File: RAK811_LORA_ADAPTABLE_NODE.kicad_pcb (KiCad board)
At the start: 2 copper layers, 75 x 49 mm, 6 parts

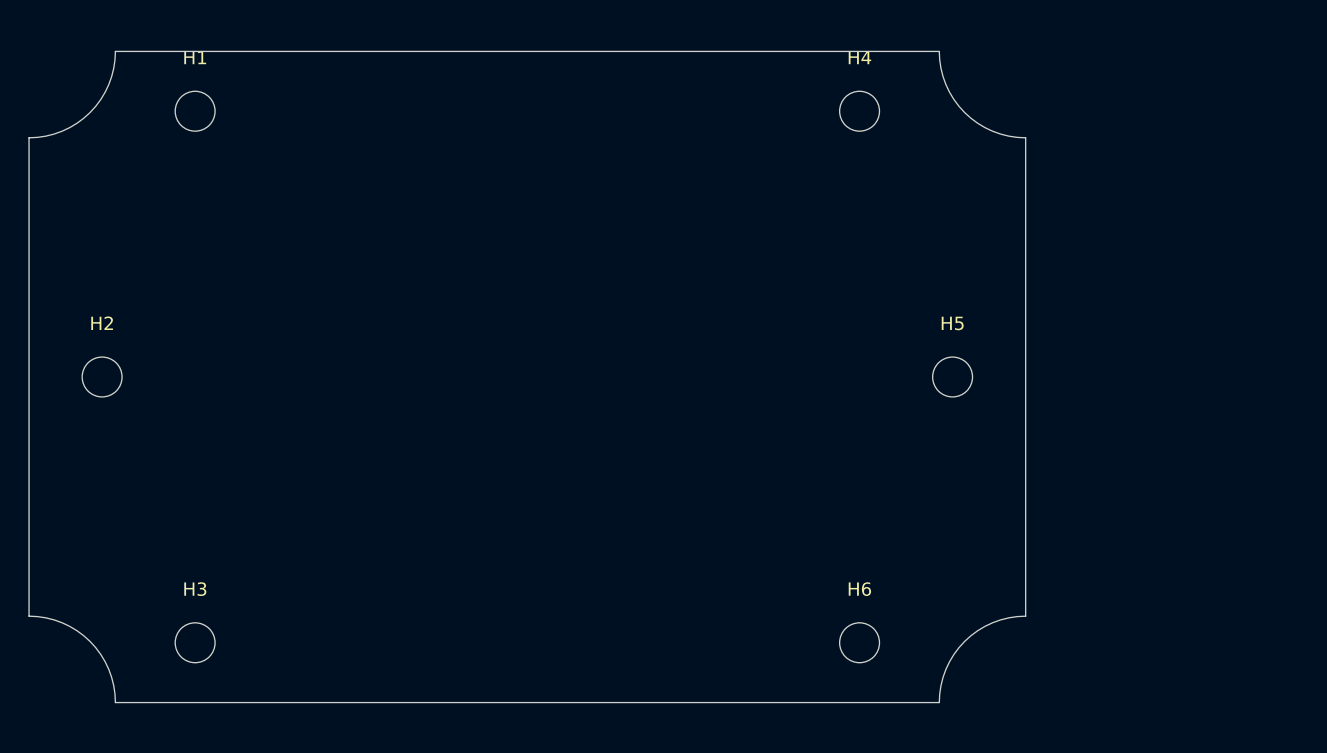
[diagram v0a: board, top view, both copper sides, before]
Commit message: put basic elements: lora mudule, battery holders, screw connectors
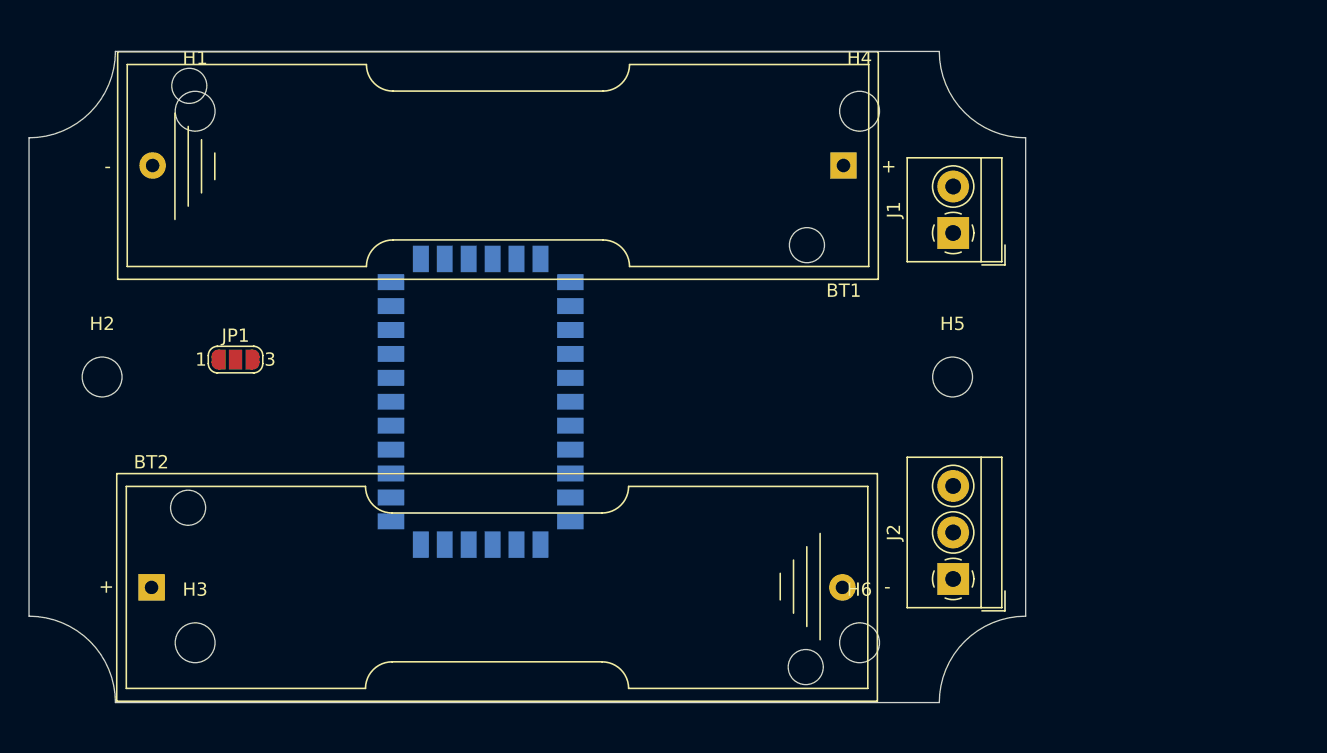
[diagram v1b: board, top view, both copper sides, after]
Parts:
- added BT1: Battery_Cell, Battery:BatteryHolder_Keystone_2460_1xAA, F.Cu at (161.3, 108.6)
- added BT2: Battery_Cell, Battery:BatteryHolder_Keystone_2460_1xAA, F.Cu at (109.2, 140.3)
- added J1: Screw_Terminal_01x02, TerminalBlock_4Ucon:TerminalBlock_4Ucon_1x02_P3.50mm_Horizontal, F.Cu at (169.5, 113.7)
- added J2: Screw_Terminal_01x03, TerminalBlock_4Ucon:TerminalBlock_4Ucon_1x03_P3.50mm_Horizontal, F.Cu at (169.5, 139.7)
- added JP1: SolderJumper_3_Open, Jumper:SolderJumper-3_P1.3mm_Open_RoundedPad1.0x1.5mm_NumberLabels, F.Cu at (115.5, 123.2)
- added U1: RAK811-HF, RF_Module:RAK811, B.Cu at (134.0, 126.4)

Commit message: RAK811 updated with improved pin1 silkscreen
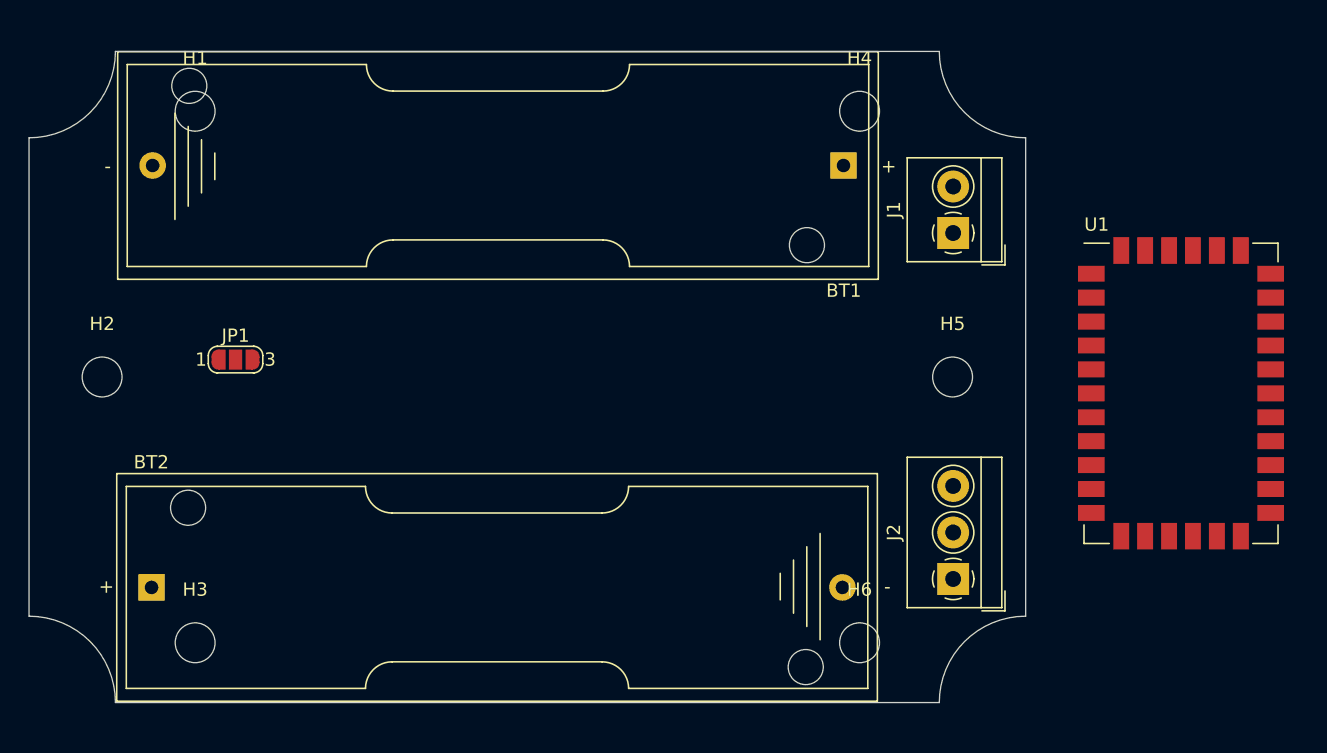
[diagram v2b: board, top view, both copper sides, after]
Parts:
- U1: moved to F.Cu
- moved U1 52.7 mm to (186.7, 125.7)

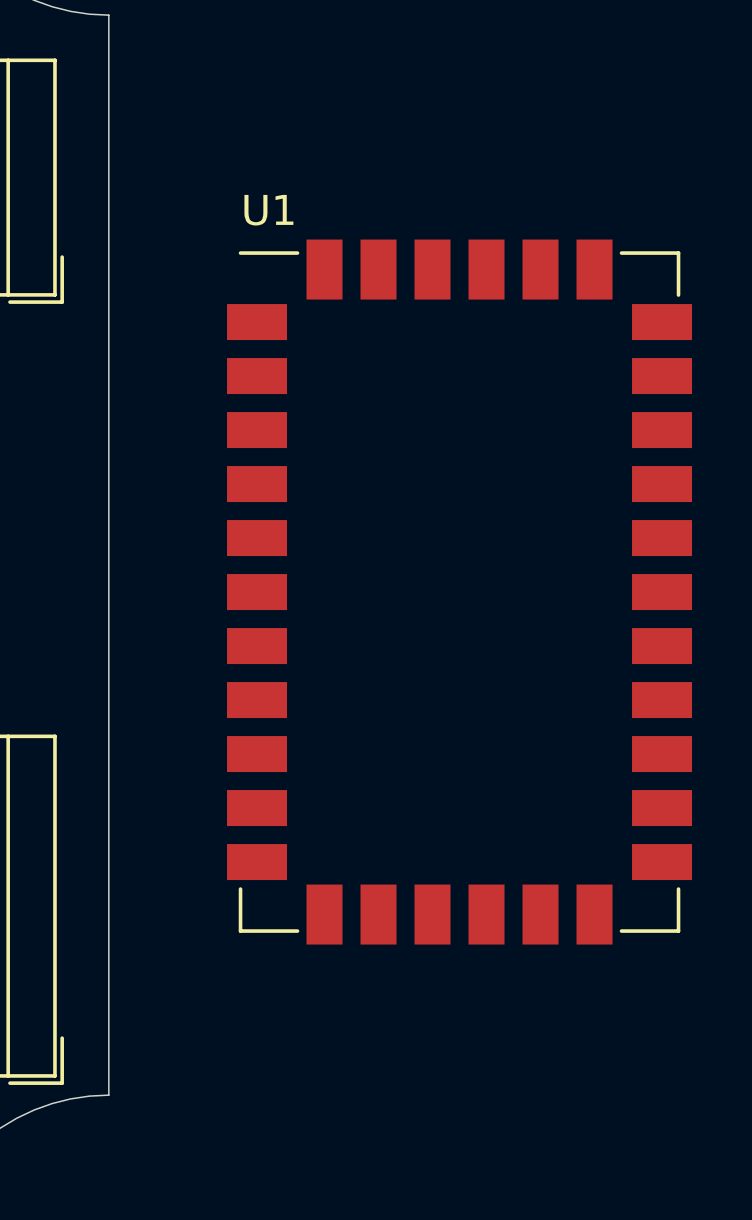
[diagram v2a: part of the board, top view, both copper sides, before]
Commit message: RAK811 updated with improved pin1 fab layer
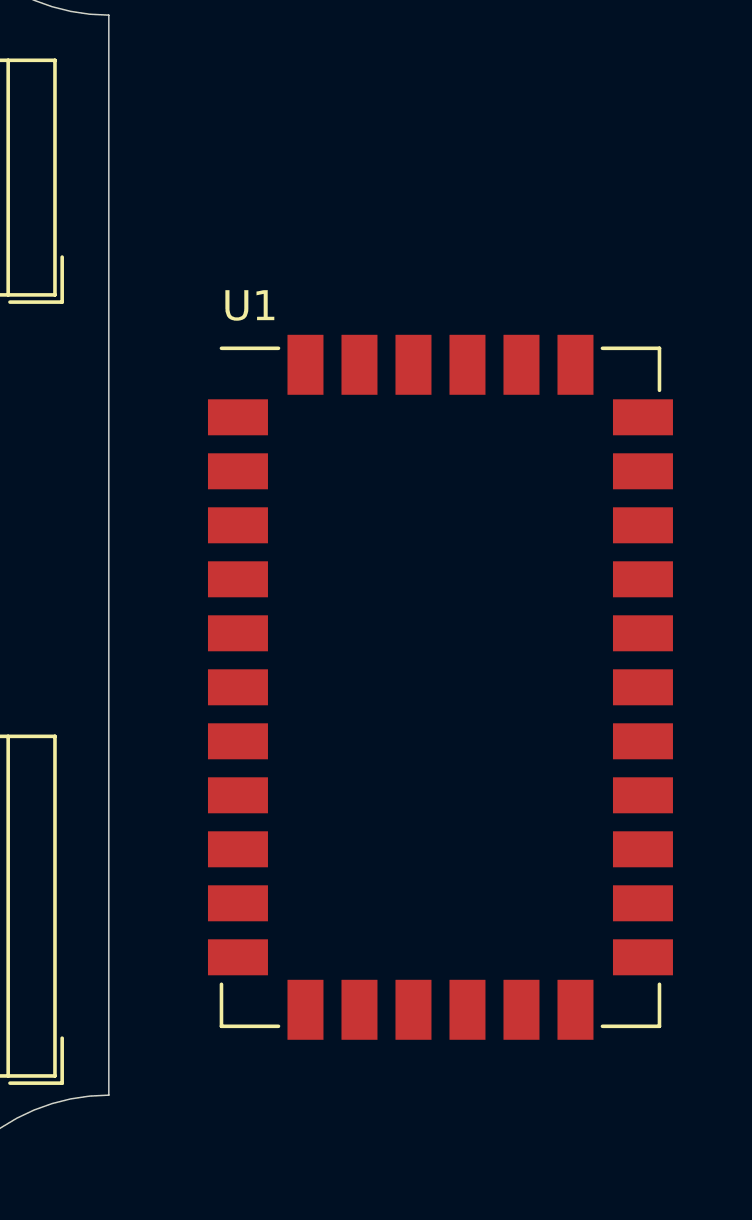
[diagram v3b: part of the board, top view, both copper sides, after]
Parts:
- moved U1 3.24 mm to (186.1, 128.9)
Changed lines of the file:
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@@
   )
   (module RF_Module:RAK811 (layer F.Cu)
-    (at 186.69 125.73)
+    (at 186.055 128.905)
     (descr "RAK811 LPWAN Module")
     (tags "LoRa LoRaWAN RAK811")
@@
       (effects (font (size 1 1) (thickness 0.15)))
     )
+    (fp_line (start -6.293 -11) (end -7 -10.293) (layer F.Fab) (width 0.12))
     (fp_text user %R (at 0 0) (layer F.Fab)
       (effects (font (size 1 1) (thickness 0.15)))
     )
-    (fp_line (start 7 -11) (end -7 -11) (layer F.Fab) (width 0.1))
+    (fp_line (start 7 -11) (end -6.293 -11) (layer F.Fab) (width 0.1))
     (fp_line (start 7 -11) (end 7 11) (layer F.Fab) (width 0.1))
     (fp_line (start 7 11) (end -7 11) (layer F.Fab) (width 0.1))
-    (fp_line (start -7 -11) (end -7 11) (layer F.Fab) (width 0.1))
+    (fp_line (start -7 -10.293) (end -7 11) (layer F.Fab) (width 0.1))
     (fp_line (start -5.4 11.3) (end -7.3 11.3) (layer F.SilkS) (width 0.12))
     (fp_line (start -7.3 11.3) (end -7.3 9.9) (layer F.SilkS) (width 0.12))

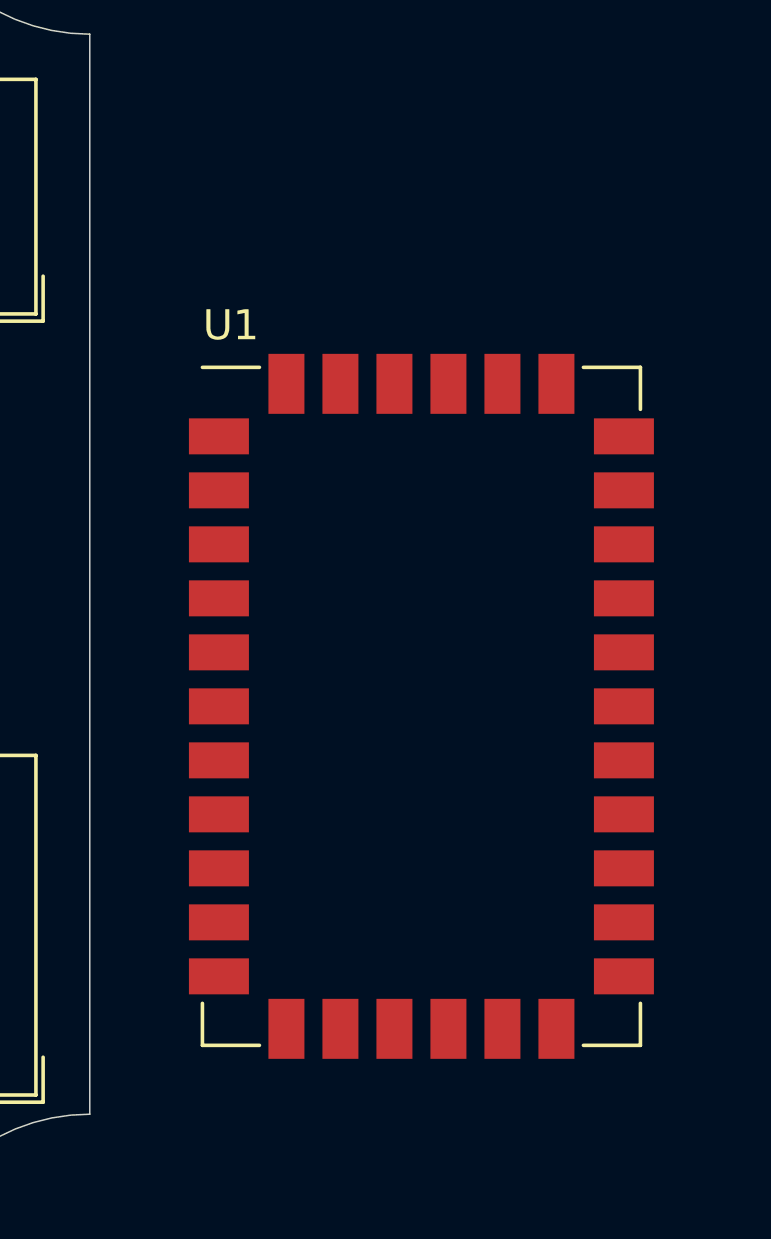
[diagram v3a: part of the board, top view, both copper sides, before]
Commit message: RAK811 updated datasheet link to FP description
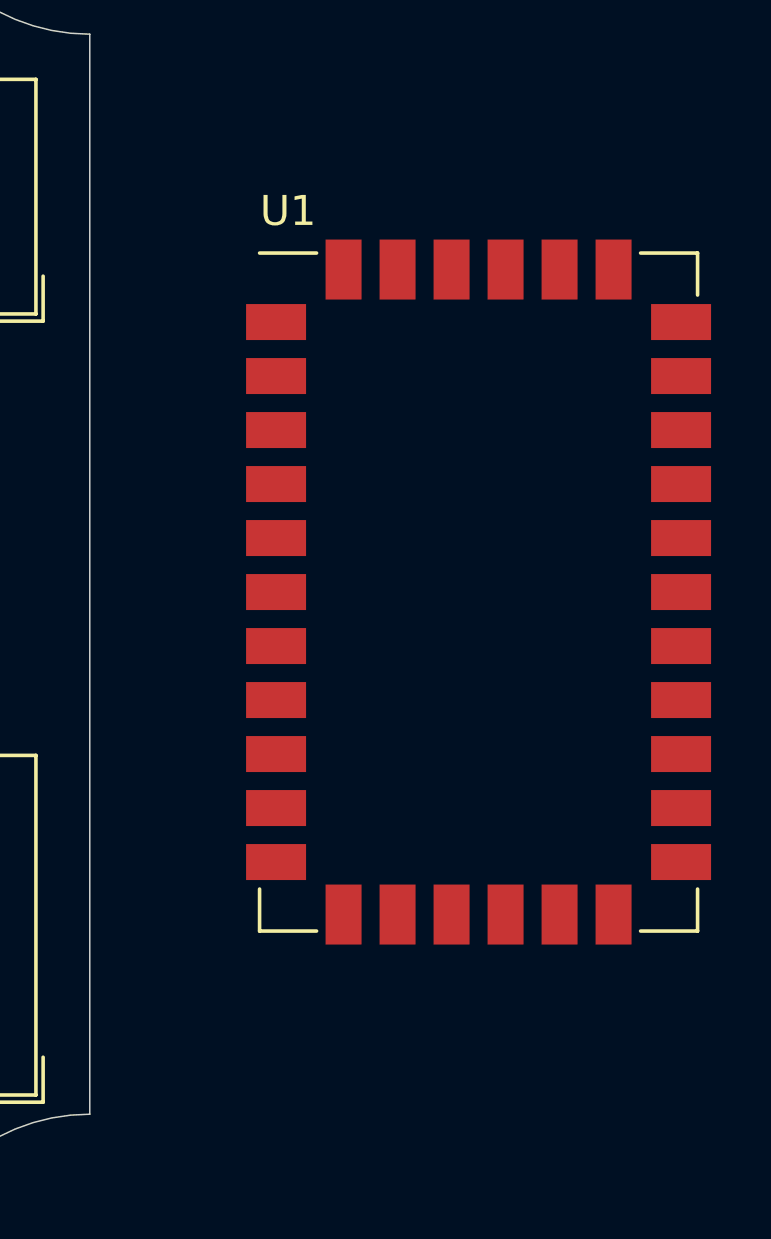
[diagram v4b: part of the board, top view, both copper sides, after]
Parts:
- moved U1 4.26 mm to (188.0, 125.1)
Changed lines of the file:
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@@
   )
   (module RF_Module:RAK811 (layer F.Cu)
-    (at 186.055 128.905)
-    (descr "RAK811 LPWAN Module")
+    (at 187.96 125.095)
+    (descr "RAK811 LPWAN Module https://downloads.rakwireless.com/LoRa/RAK811/Hardware_Specification/RAK811_LoRa_Module_Datasheet_V1.4.pdf")
     (tags "LoRa LoRaWAN RAK811")
     (attr smd)

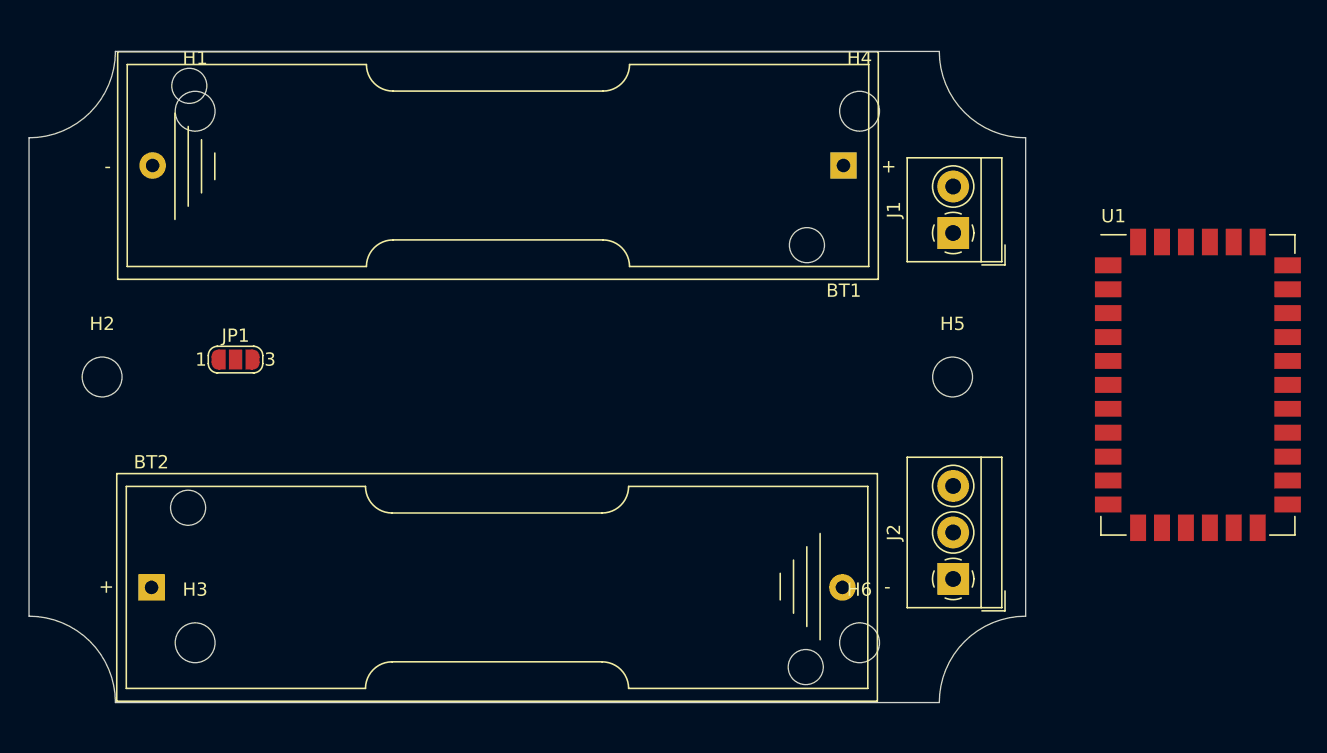
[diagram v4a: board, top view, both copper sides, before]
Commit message: add antenna output connectors
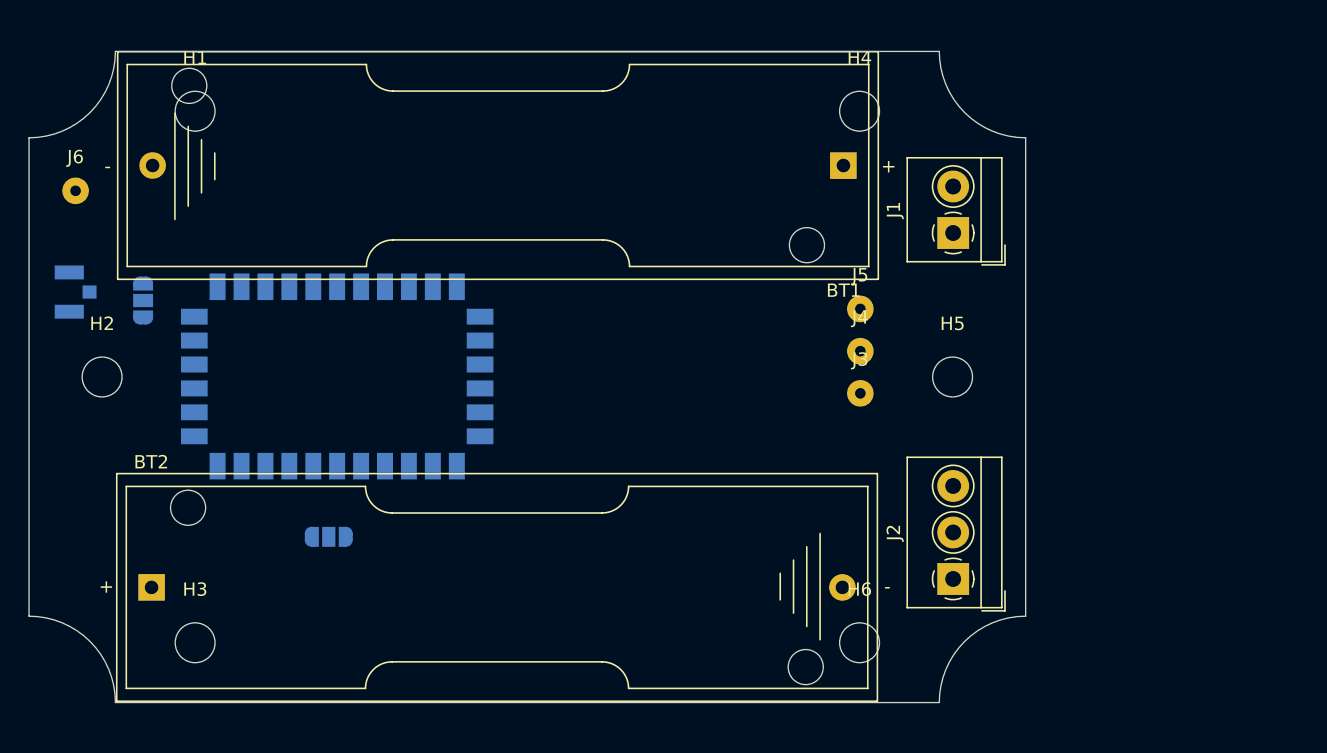
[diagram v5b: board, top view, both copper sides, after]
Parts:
- added J3: Conn_01x01_Male, Connector_Wire:SolderWirePad_1x01_Drill0.8mm, F.Cu at (162.6, 125.7)
- added J4: Conn_01x01_Male, Connector_Wire:SolderWirePad_1x01_Drill0.8mm, F.Cu at (162.6, 122.6)
- added J5: Conn_01x01_Male, Connector_Wire:SolderWirePad_1x01_Drill0.8mm, F.Cu at (162.6, 119.4)
- added J6: Conn_01x01_Male, Connector_Wire:SolderWirePad_1x01_Drill0.8mm, F.Cu at (103.5, 110.5)
- added J7: Conn_Coaxial, Connector_Coaxial:U.FL_Hirose_U.FL-R-SMT-1_Vertical, B.Cu at (103.5, 118.1)
- added JP2: SolderJumper_3_Open, Jumper:SolderJumper-3_P1.3mm_Open_RoundedPad1.0x1.5mm_NumberLabels, B.Cu at (108.6, 118.7)
- JP1, U1: moved to B.Cu
- moved U1 64.8 mm to (123.2, 124.5), turned to 270 degrees
- moved JP1 15.1 mm to (122.6, 136.5)
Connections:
- J1 pad 2: Net-(J1-Pad2) -> Net-(BT2-Pad2)
- JP1 pad 2: Net-(JP1-Pad2) -> Net-(J1-Pad1)
- U1 pad 11: Net-(JP1-Pad2) -> Net-(J1-Pad1)
